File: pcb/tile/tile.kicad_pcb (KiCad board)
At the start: 2 copper layers, 21.4 x 30.7 mm, 15 parts, among them IC1 THVD1420DR, J1 LED Strip, J2 UPDI, J5 12V, J6 RS-485 Jack, U1 ATtiny3224-X

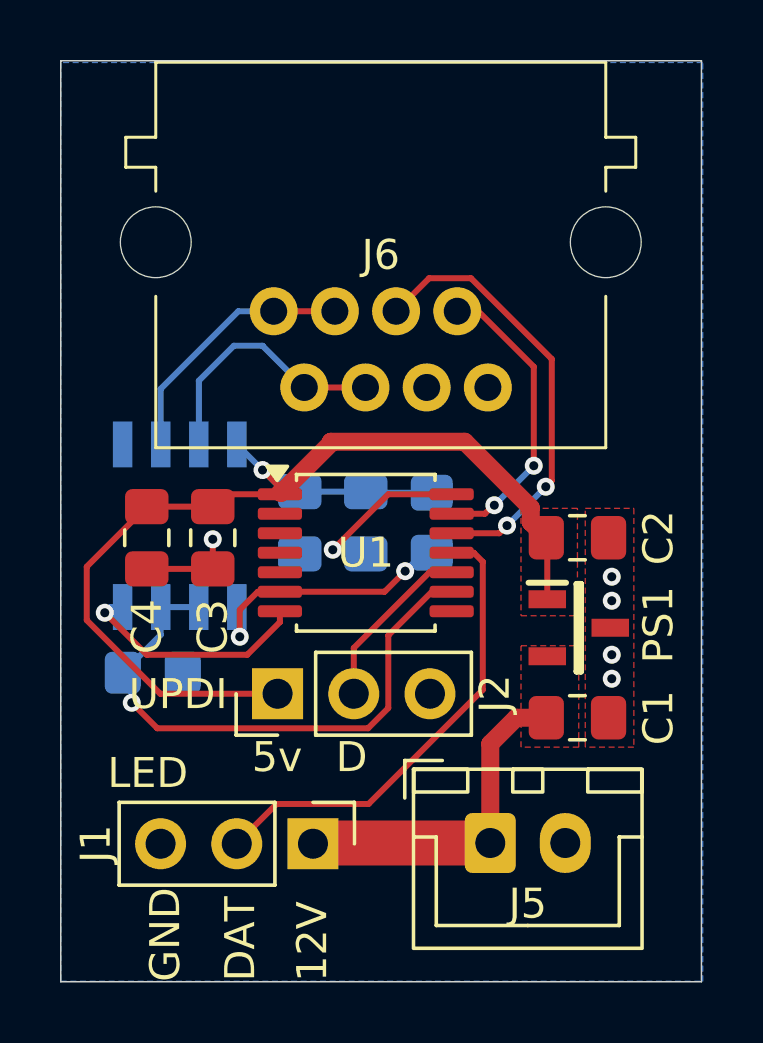
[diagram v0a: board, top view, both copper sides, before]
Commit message: Updated to account for a bulk cap as well as a resistor on the LED data line
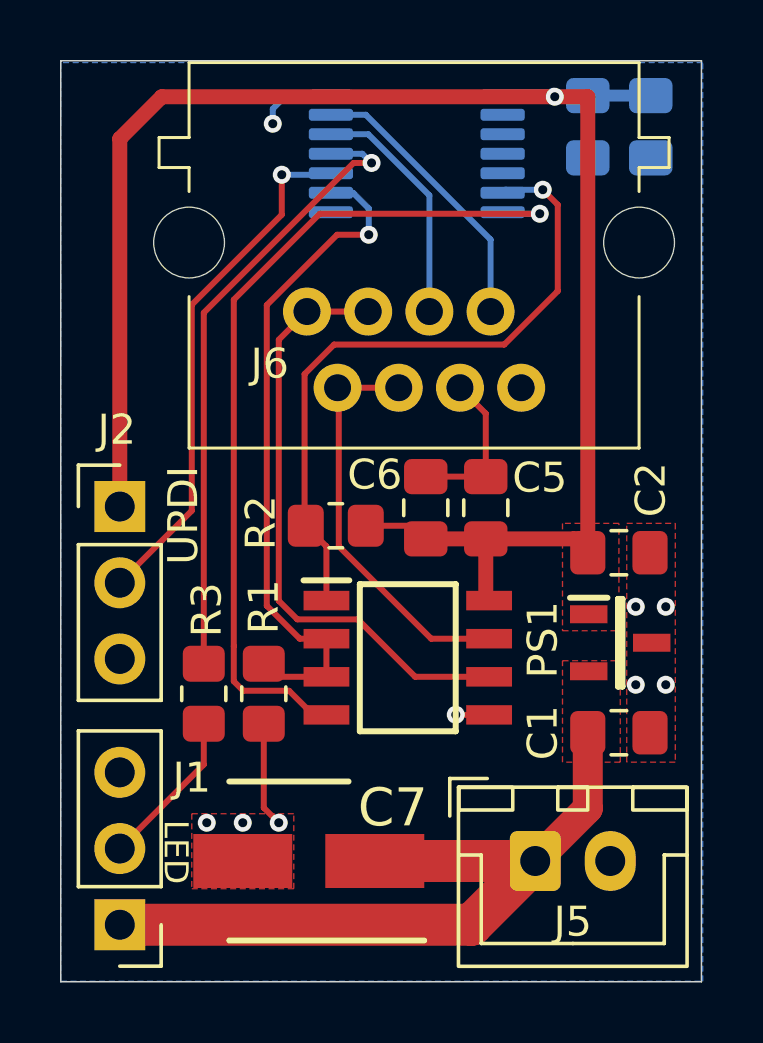
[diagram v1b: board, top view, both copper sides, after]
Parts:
- added C7: 865080342006, Garth:CAPAE530X550N, F.Cu at (148.8, 91.4)
- added R3: 330, Resistor_SMD:R_0805_2012Metric_Pad1.20x1.40mm_HandSolder, F.Cu at (145.3, 85.8)
- C3, C4, U1: moved to B.Cu
- C5, C6, IC1, R1, R2: moved to F.Cu
- moved C4 21.7 mm to (160.2, 66.9)
- moved C3 18.5 mm to (158.1, 66.9)
- moved U1 13.4 mm to (152.4, 67.8), turned to 180 degrees
- moved IC1 8.78 mm to (152.1, 84.6), turned to 0 degrees
- moved J2 8.16 mm to (142.5, 79.6), turned to 0 degrees
- moved J1 6.98 mm to (142.5, 93.5), turned to 180 degrees
- moved C5 6.22 mm to (154.7, 79.6), turned to 90 degrees
- moved R1 3.77 mm to (147.3, 85.8), turned to -90 degrees
- moved R2 3.20 mm to (149.7, 80.2), turned to 180 degrees
- moved C6 2.06 mm to (152.7, 79.6), turned to 90 degrees
- moved J5 1.62 mm to (156.3, 91.4)
- moved C1 1.47 mm to (159.1, 87.1)
- moved C2 1.47 mm to (159.1, 81.1)
- moved PS1 1.47 mm to (159.2, 84.1)
- moved J6 1.11 mm to (152.3, 73.1)
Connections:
- J1 pad 2: /LED_Data -> Net-(J1-Pin_2)
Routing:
- net +5V: track 38.0 -> 59.4 mm
- net /TxD: track 7.90 -> 28.9 mm
- net +12V: track 11.5 -> 25.1 mm
- net /RxD: track 9.26 -> 22.4 mm, vias 2 -> 1
- net /UDPI_Data: track 5.83 -> 17.5 mm, vias 0 -> 1
- net /TRCV-A: track 8.73 -> 20.1 mm
- net /SENSE_IN: track 14.9 -> 8.00 mm, vias 2 -> 0
- net Net-(J1-Pin_2): track 0.00 -> 5.32 mm
- net /LED_Data: track 15.8 -> 20.8 mm, vias 0 -> 1
- net /TRCV-B: track 8.74 -> 13.8 mm
- net GND: track 7.92 -> 12.6 mm, vias 6 -> 9
- net /XDIR: track 19.4 -> 22.7 mm
- net /SENSE_OUT: track 10.0 -> 9.45 mm, vias 2 -> 0
